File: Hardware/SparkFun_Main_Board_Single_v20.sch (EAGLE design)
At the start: 84 parts, among them J1 MICROMOD-2222-C, J10 MICRO-SD-PUSH-PUSH-EXT-PIN, J2 Vertical Qwiic Connector, J4 QWIIC_RIGHT_ANGLE, J5 CORTEX_JTAG_DEBUG_MINIMUM_PTH, J6 MICROMOD_FUNCTION_MAIN, Q1 3.1A/30V/105mΩ, Q2 20V/4.2A/52mΩ/1.4W, U1 STG3856QTR, U2 MCP73831, U3 ESD Diode, U4 AP7347DQ-33W5-7K-3.3V, U5 AP7361C-33

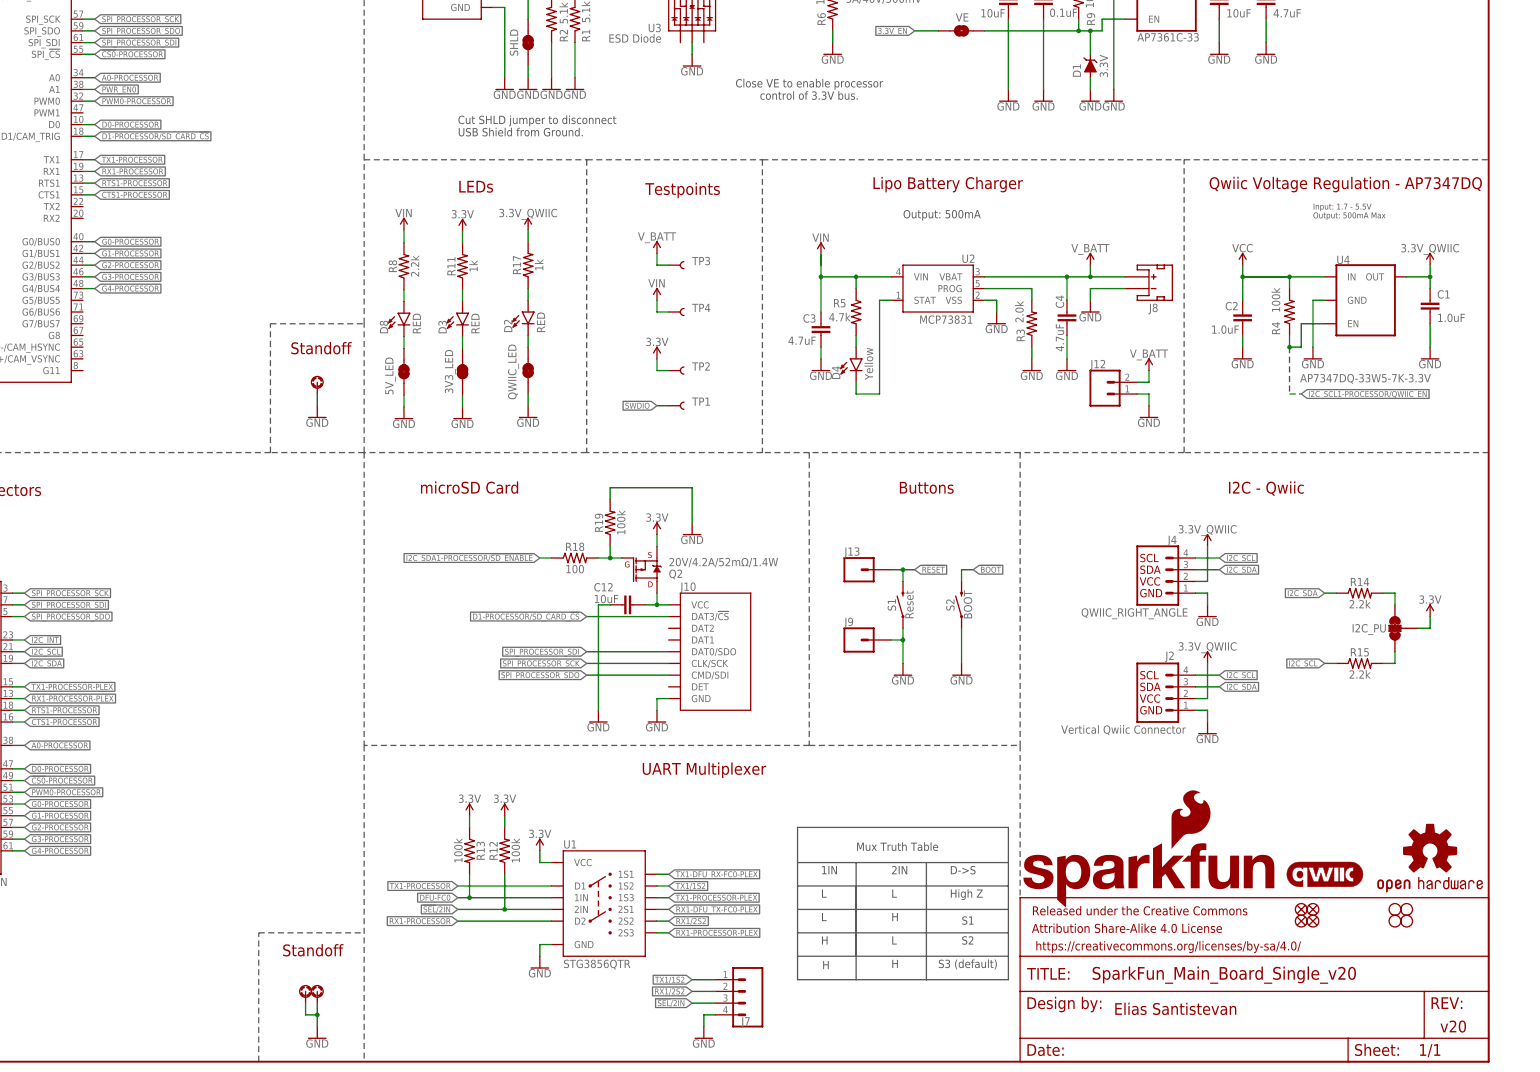
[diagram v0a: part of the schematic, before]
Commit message: Routes PWM1 pin to power enable pin on function card
* Rolls version to v21
* Fixes PTC silk
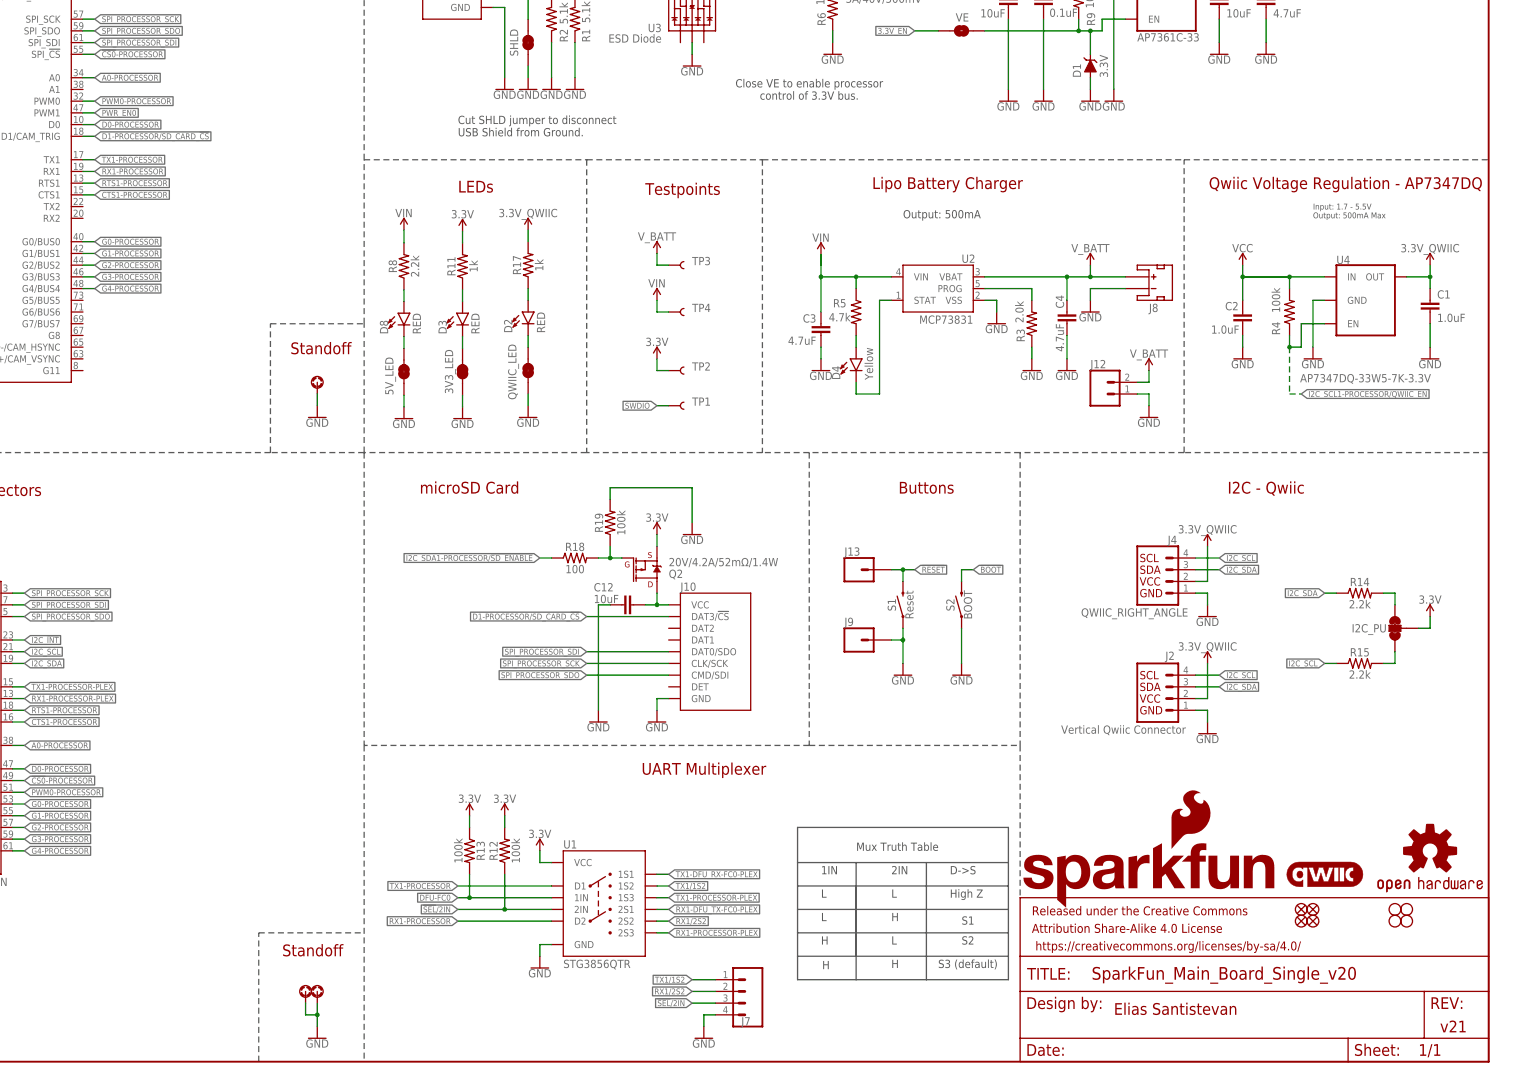
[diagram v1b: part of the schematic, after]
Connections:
- net PWR_EN0: now also J1.PWM1; no longer J1.A1
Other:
- note added: "v21"
- note removed: "v20"
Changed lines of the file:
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@@
 <text x="96.774" y="123.952" size="2.54" layer="94" font="vector" align="center">Function Board Connectors</text>
 <text x="95.25" y="271.526" size="2.54" layer="94" font="vector" align="center">Processor Board Connector</text>
-<text x="424.18" y="7.62" size="2.54" layer="94" font="vector" align="center">v20</text>
+<text x="424.18" y="7.62" size="2.54" layer="94" font="vector" align="center">v21</text>
 <wire x1="365.76" y1="132.08" x2="330.2" y2="132.08" width="0.2032" layer="97" style="longdash"/>
 <wire x1="330.2" y1="132.08" x2="284.48" y2="132.08" width="0.2032" layer="97" style="longdash"/>
@@
 <net name="PWR_EN0" class="0">
 <segment>
-<wire x1="129.54" y1="210.82" x2="127" y2="210.82" width="0.1524" layer="91"/>
-<pinref part="J1" gate="J1" pin="A1"/>
-<label x="129.54" y="210.82" size="1.27" layer="95" font="vector" xref="yes"/>
-</segment>
-<segment>
 <wire x1="76.2" y1="93.98" x2="73.66" y2="93.98" width="0.1524" layer="91"/>
 <label x="73.66" y="93.98" size="1.27" layer="95" font="vector" rot="R180" xref="yes"/>
 <pinref part="J6" gate="J1" pin="PWR_EN"/>
 </segment>
-</net>
+<segment>
+<wire x1="129.54" y1="205.74" x2="127" y2="205.74" width="0.1524" layer="91"/>
+<label x="129.54" y="205.74" size="1.27" layer="95" font="vector" xref="yes"/>
+<pinref part="J1" gate="J1" pin="PWM1"/>
+</segment>
+</net>
